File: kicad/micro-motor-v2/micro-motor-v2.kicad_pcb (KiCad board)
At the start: 2 copper layers, 35 x 20 mm, 72 parts, among them J101 SUPPLY, J102 SW, J103 Hall, J104 Encoder, J105 NTC, J106 Motor, J201 CAN, J301 USB, J302 UART, J303 SWD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

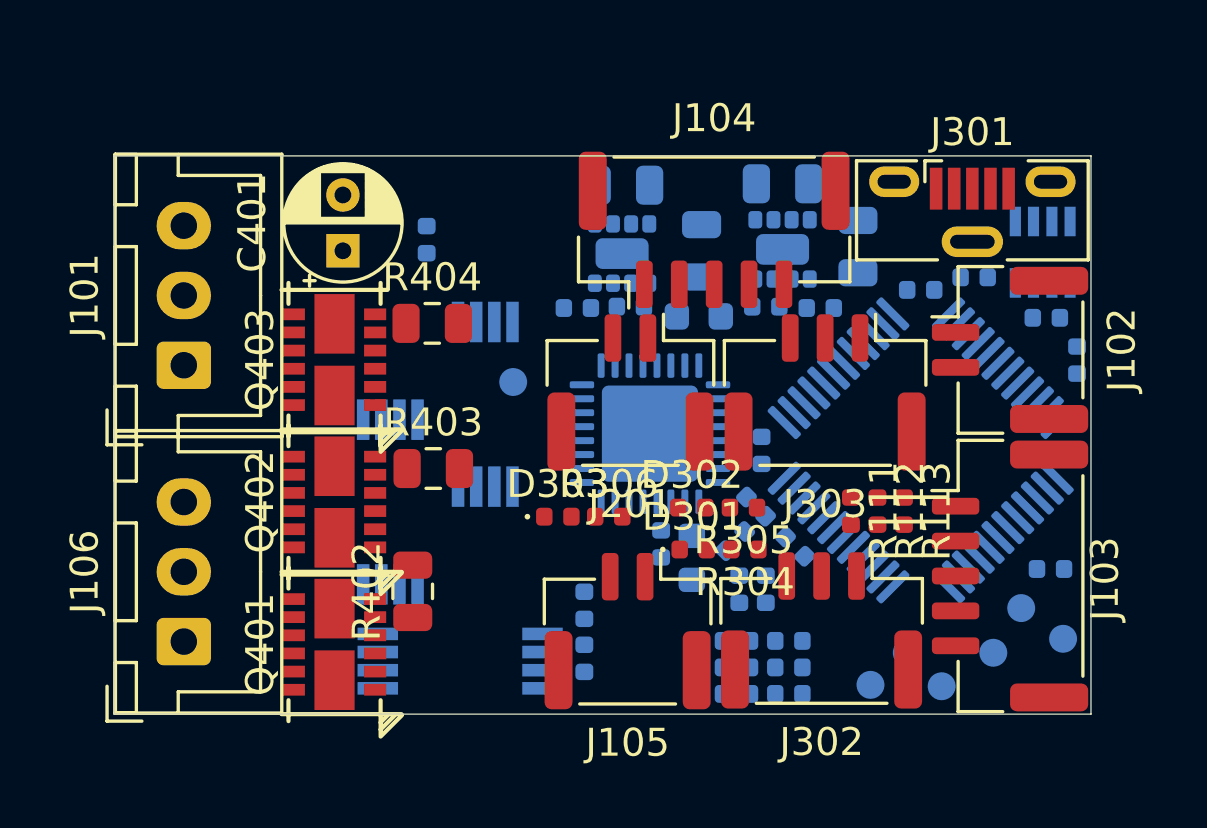
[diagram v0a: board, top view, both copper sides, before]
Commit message: micro-motor-v2: More capacitors, outline corners
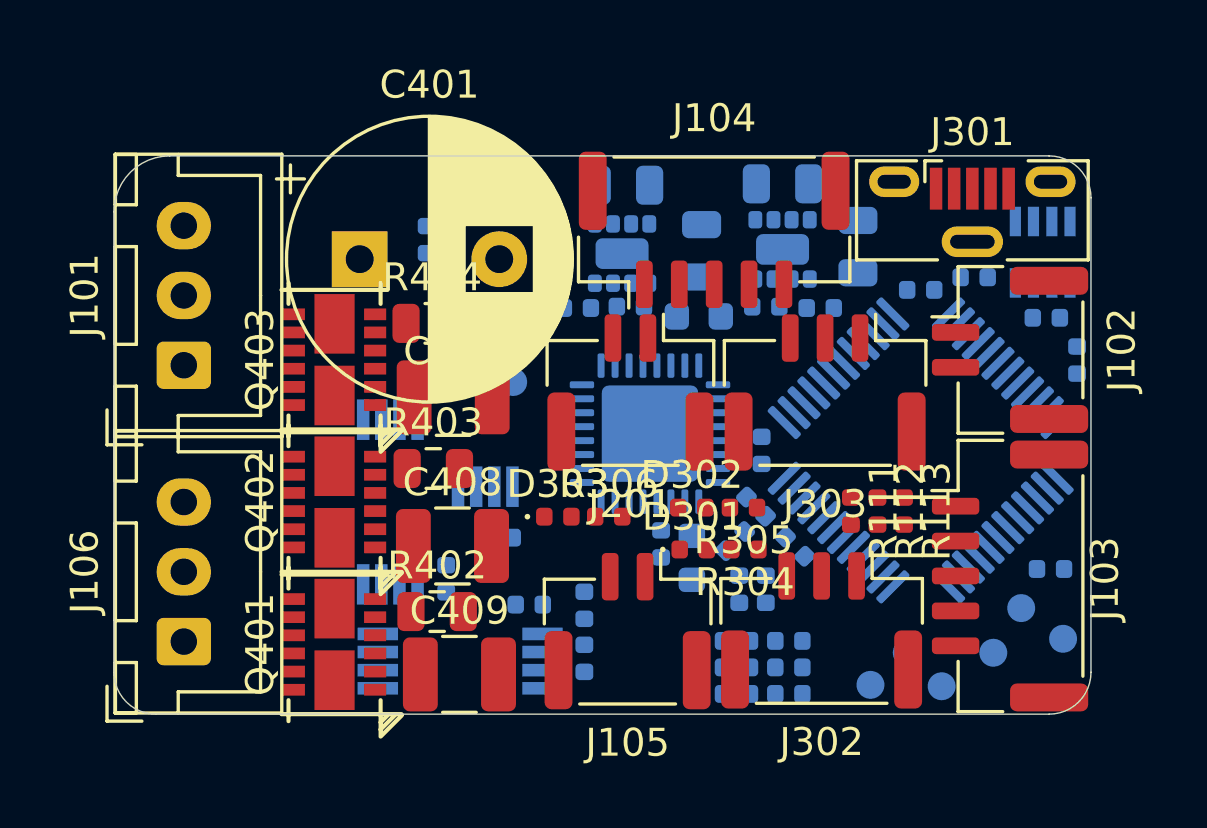
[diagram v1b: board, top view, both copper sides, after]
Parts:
- added C407: 22µ 35V 1210, Capacitor_SMD:C_1210_3225Metric, F.Cu at (162.2, 108.7)
- added C408: 22µ 35V 1210, Capacitor_SMD:C_1210_3225Metric, F.Cu at (162.1, 114.0)
- added C409: 22µ 35V 1210, Capacitor_SMD:C_1210_3225Metric, F.Cu at (162.4, 118.6)
- added C410: 100n, Capacitor_SMD:C_0402_1005Metric, B.Cu at (164.9, 116.1)
- added C411: 100n, Capacitor_SMD:C_0402_1005Metric, B.Cu at (161.9, 115.2)
- added C412: 100n, Capacitor_SMD:C_0402_1005Metric, B.Cu at (163.8, 113.7)
- C401: footprint Capacitor_THT:CP_Radial_D4.0mm_P2.00mm -> Capacitor_THT:CP_Radial_D10.0mm_P5.00mm
- C402, C403: value 100n 50V -> 100n
- moved R402 1.14 mm to (161.6, 116.3), turned to 0 degrees
- moved C401 0.67 mm to (158.8, 103.7), turned to 0 degrees
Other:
- outline, holes or cut-outs redrawn

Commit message: micro-motor-v2: Layout...
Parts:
- added R114: 0, Resistor_SMD:R_0402_1005Metric, F.Cu at (165.4, 101.2)
- moved J102 13.8 mm to (168.4, 108.5), turned to 180 degrees
- moved J201 13.7 mm to (182.1, 106.7), turned to 270 degrees
- moved TP303 3.96 mm to (179.7, 119.0)
- moved TP103 2.89 mm to (182.4, 118.1)
- moved TP401 2.11 mm to (166.1, 107.0)
- moved C504 1.89 mm to (169.9, 101.9)
- moved TP102 1.86 mm to (182.6, 116.3)
- moved C503 1.77 mm to (175.5, 101.9)
- moved C402 1.27 mm to (168.7, 114.8), turned to 180 degrees
- moved D303 1.20 mm to (167.0, 113.4)
- moved R306 1.18 mm to (168.8, 113.4), turned to 180 degrees
- moved R501 1.07 mm to (175.1, 104.4), turned to 270 degrees
- moved C502 1.00 mm to (172.9, 101.0)
- moved U501 1.00 mm to (172.9, 103.3)
- moved C501 0.90 mm to (167.3, 101.0)
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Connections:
- net Net-(J201-Pad1) renamed /Can/CANH
- net Net-(J201-Pad2) renamed /Can/CANL
- net Net-(Q401-Pad14) renamed /Motordriver/GND_A
- net Net-(Q402-Pad14) renamed /Motordriver/GND_B
- net Net-(Q403-Pad14) renamed /Motordriver/GND_C
- C401 pad 2: GND -> GNDPWR
- C402 pad 2: GND -> GNDPWR
- C403 pad 2: GND -> GNDPWR
- C404 pad 2: GND -> GNDPWR
- C407 pad 2: GND -> GNDPWR
- C408 pad 2: GND -> GNDPWR
- C409 pad 2: GND -> GNDPWR
- J101 pad 2: GND -> GNDPWR
- R402 pad 2: GND -> GNDPWR
- R403 pad 2: GND -> GNDPWR
- R404 pad 2: GND -> GNDPWR
- U301 pad 17: /Microcontroller/ADC_Vsupply -> /Microcontroller/ADC_NTC
- U301 pad 18: /Microcontroller/ADC_NTC -> /Microcontroller/ADC_Vsupply
- U401 pad 23: GND -> GNDPWR
- U401 pad 31: GND -> GNDPWR
- U401 pad 33: GND -> GNDPWR
- U402 pad 3: GND -> GNDPWR
- U403 pad 3: GND -> GNDPWR
- U404 pad 3: GND -> GNDPWR
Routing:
- net GND: track 0.00 -> 94.3 mm, vias 0 -> 6
- net GNDPWR: track 0.00 -> 32.9 mm, vias 0 -> 6
- net +3V3: track 0.00 -> 26.3 mm, vias 0 -> 2
- net Net-(Q401-Pad12): track 0.00 -> 17.3 mm, vias 0 -> 2
- net /Motordriver/OUT_U: track 0.00 -> 15.9 mm, vias 0 -> 2
- net +24V: track 0.00 -> 15.6 mm, vias 0 -> 35
- net /Microcontroller/B: track 0.00 -> 15.5 mm, vias 0 -> 1
- net /Microcontroller/DAC2: track 0.00 -> 14.5 mm, vias 0 -> 1
- net /Motordriver/OUT_V: track 0.00 -> 14.3 mm, vias 0 -> 2
- net /Microcontroller/A: track 0.00 -> 14.0 mm, vias 0 -> 1
- net Net-(Q402-Pad12): track 0.00 -> 13.0 mm, vias 0 -> 2
- net /Motordriver/OUT_W: track 0.00 -> 12.1 mm, vias 0 -> 2
- net /Microcontroller/DAC1: track 0.00 -> 12.0 mm, vias 0 -> 1
- net /Motordriver/GND_A: track 0.00 -> 11.8 mm, vias 0 -> 2
- net /Microcontroller/INDEX: track 0.00 -> 11.8 mm, vias 0 -> 1
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- added copper zone on F.Cu, net +24V
- added copper zone on In1.Cu, net +24V
- added copper zone on F.Cu, net /Motordriver/GND_A
- added copper zone on F.Cu, net /Motordriver/GND_B
- added copper zone on F.Cu, net /Motordriver/GND_C
- added copper zone on F.Cu, net /Motordriver/OUT_U
- added copper zone on F.Cu, net /Motordriver/OUT_V
- added copper zone on F.Cu, net /Motordriver/OUT_W
- added copper zone on F.Cu, net GND
- added copper zone on In1.Cu, net GND
- added copper zone on F.Cu, net GNDPWR
- added copper zone on In1.Cu, net GNDPWR
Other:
- copper layers 2 -> 4
- rule pad_to_mask_clearance: 0.051 -> 0.025
- rule solder_mask_min_width: 0.25 -> 0.1
- rule trace_min: 0.2 -> 0.125
- rule via_min_drill: 0.3 -> 0.2
- rule via_min_size: 0.4 -> 0.3

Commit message: micro-motor-v2: Layout...
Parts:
- moved R401 8.71 mm to (165.6, 106.3), turned to 270 degrees
- moved R504 4.37 mm to (170.5, 104.3), turned to 90 degrees
- moved R502 4.34 mm to (177.1, 102.8), turned to 90 degrees
- moved TP401 2.89 mm to (163.8, 108.8)
- moved R503 1.84 mm to (169.5, 104.3), turned to 270 degrees
- moved R108 1.34 mm to (168.0, 117.8), turned to 270 degrees
- moved R105 1.05 mm to (175.2, 118.1)
- moved R103 0.80 mm to (174.6, 116.7), turned to 90 degrees
- moved R107 0.28 mm to (174.2, 119.0)
- moved C504 0.10 mm to (169.9, 101.8)
- moved C404 0.10 mm to (171.3, 105.8)
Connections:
- R102 pad 1: /Motordriver/OUT_W -> /Motordriver/OUT_U
- R102 pad 2: /Microcontroller/Volt_W -> /Microcontroller/Volt_U
- R103 pad 1: /Microcontroller/Volt_W -> /Microcontroller/Volt_U
- R106 pad 1: /Motordriver/OUT_U -> /Motordriver/OUT_W
- R106 pad 2: /Microcontroller/Volt_U -> /Microcontroller/Volt_W
- R107 pad 1: /Microcontroller/Volt_U -> /Microcontroller/Volt_W
- U301 pad 14: /Microcontroller/Volt_U -> /Microcontroller/Volt_W
- U301 pad 16: /Microcontroller/Volt_W -> /Microcontroller/Volt_U
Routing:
- net +3V3: track 26.3 -> 71.6 mm, vias 2 -> 7
- net +5V: track 0.00 -> 38.9 mm, vias 0 -> 1
- net +6V: track 0.00 -> 32.4 mm, vias 0 -> 4
- net /Microcontroller/~CS: track 0.00 -> 22.7 mm, vias 0 -> 2
- net /Microcontroller/ENABLE: track 0.00 -> 18.3 mm, vias 0 -> 2
- net /Motordriver/MOSI: track 0.00 -> 17.3 mm, vias 0 -> 2
- net /Microcontroller/VREF: track 1.61 -> 17.2 mm, vias 0 -> 2
- net /Microcontroller/B: track 15.5 -> 0.00 mm, vias 1 -> 0
- net /Motordriver/OUT_W: track 12.1 -> 27.0 mm
- net /Microcontroller/A: track 14.0 -> 0.00 mm, vias 1 -> 0
- net /Motordriver/SCK: track 0.00 -> 12.4 mm, vias 0 -> 2
- net /Microcontroller/INDEX: track 11.8 -> 0.00 mm, vias 1 -> 0
- net /Motordriver/MISO: track 1.02 -> 12.1 mm, vias 0 -> 2
- net /Motordriver/OUT_V: track 14.3 -> 25.1 mm
- net /Motordriver/IN_W_P: track 0.00 -> 9.10 mm, vias 0 -> 2
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
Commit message: micro-motor-v2: Layout...
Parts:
- moved R103 2.77 mm to (171.8, 116.3), turned to 180 degrees
- moved C403 0.71 mm to (161.3, 103.7), turned to 0 degrees
- moved R109 0.30 mm to (171.8, 115.4)
- moved C411 0.30 mm to (162.2, 114.9)
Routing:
- net /Microcontroller/Curr_V: track 0.00 -> 33.0 mm, vias 0 -> 2
- net /Microcontroller/Curr_W: track 0.00 -> 26.3 mm, vias 0 -> 2
- net /Microcontroller/Curr_U: track 0.00 -> 22.0 mm, vias 0 -> 2
- net /Microcontroller/B: track 0.00 -> 20.0 mm, vias 0 -> 1
- net /Microcontroller/SWITCH: track 2.43 -> 21.3 mm, vias 0 -> 2
- net /Microcontroller/UART_TX: track 0.00 -> 17.2 mm, vias 0 -> 2
- net /Microcontroller/A: track 0.00 -> 15.5 mm, vias 0 -> 1
- net /Microcontroller/INDEX: track 0.00 -> 14.1 mm, vias 0 -> 1
- net /Microcontroller/UART_RX: track 0.00 -> 13.8 mm, vias 0 -> 2
- net GND: track 102.5 -> 115.0 mm, vias 12 -> 15
- net +3V3: track 71.6 -> 82.0 mm, vias 7 -> 10
- net /Microcontroller/ADC_NTC: track 4.02 -> 12.8 mm, vias 1 -> 2
- net /Microcontroller/SWCLK: track 4.68 -> 7.80 mm
- net GNDPWR: track 32.7 -> 35.0 mm
- net +24V: track 15.6 -> 17.6 mm, vias 35 -> 33
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
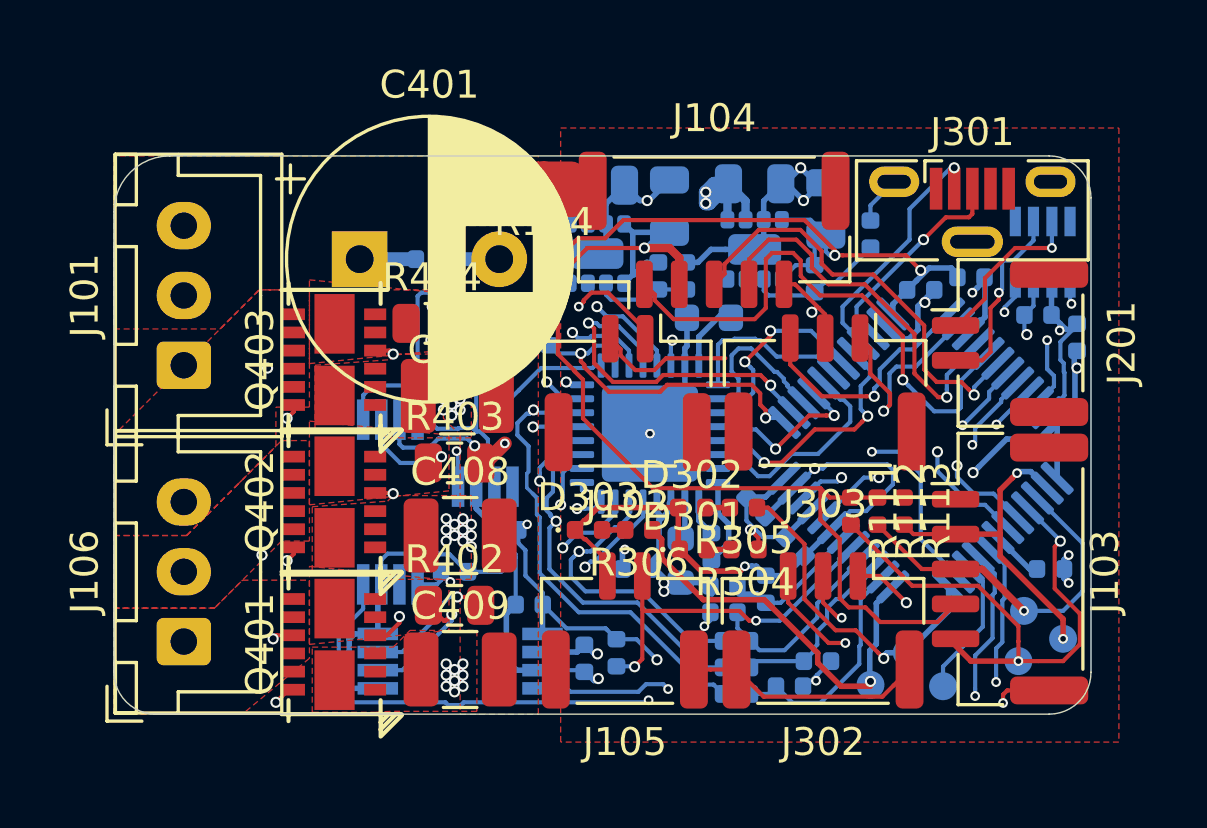
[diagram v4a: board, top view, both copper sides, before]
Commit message: micro-motor-v2: Layout finished
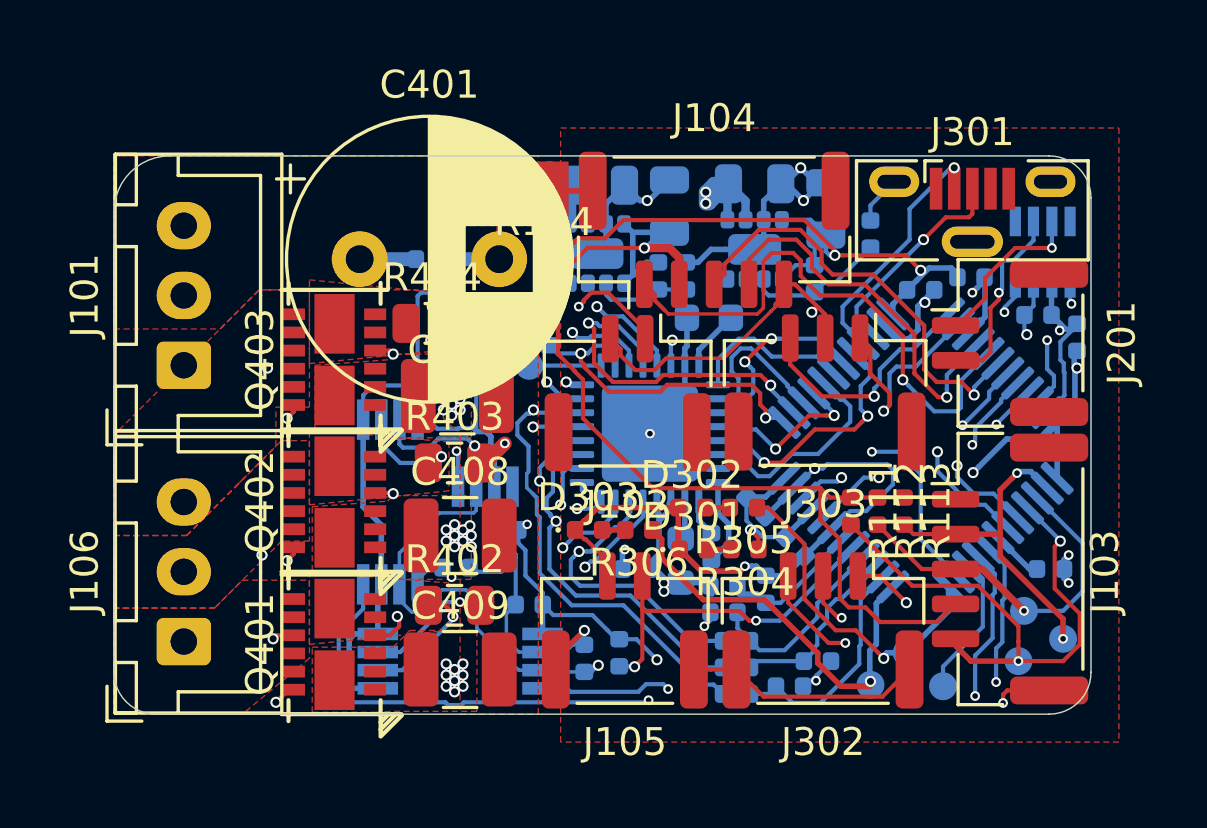
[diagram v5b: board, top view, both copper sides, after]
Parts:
- moved TP401 1.63 mm to (164.9, 107.5)
- moved C411 0.16 mm to (162.2, 114.8)
- moved R108 0.10 mm to (168.1, 117.8)
- turned C302 to 90 degrees
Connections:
- U402 pad 6: /Microcontroller/VREF -> GND
- U402 pad 7: GND -> /Microcontroller/VREF
- U404 pad 6: /Microcontroller/VREF -> GND
- U404 pad 7: GND -> /Microcontroller/VREF
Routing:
- net /Microcontroller/VREF: track 18.2 -> 31.6 mm
- net GND: track 115.0 -> 122.2 mm
- net GNDPWR: track 35.0 -> 37.4 mm
- net Net-(TP401-Pad1): track 4.16 -> 2.57 mm
- net +24V: vias 33 -> 32
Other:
- net class Default: clearance 0.2 -> 0.15
- rule trace_clearance: 0.2 -> 0.15

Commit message: micro-motor-v2: Layout Silkscreen
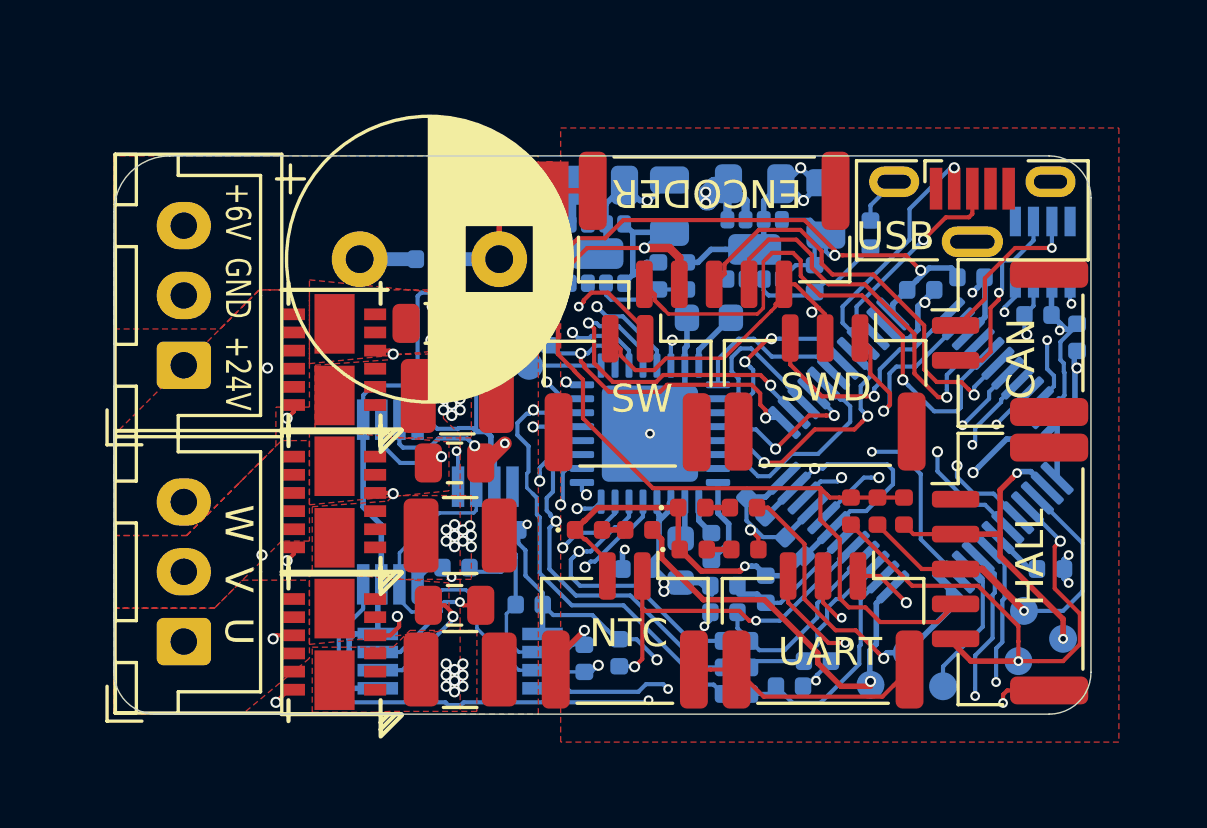
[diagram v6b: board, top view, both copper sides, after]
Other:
- board text added: "+24V"
- board text added: "+6V GND +24V"
- board text added: "BK"
- board text added: "CAN"
- board text added: "DAC1"
- board text added: "DAC2"
- board text added: "ENCODER"
- board text added: "GND"
- board text added: "HALL"
- board text added: "NTC"
- board text added: "SW"
- board text added: "SWD"
- board text added: "U"
- board text added: "UART"
- board text added: "USB"
- board text added: "V"
- board text added: "W"
- board text added: "W V U"
- board text added: "micro-motor-v2.0"
